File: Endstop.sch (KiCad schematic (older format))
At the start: 4 parts

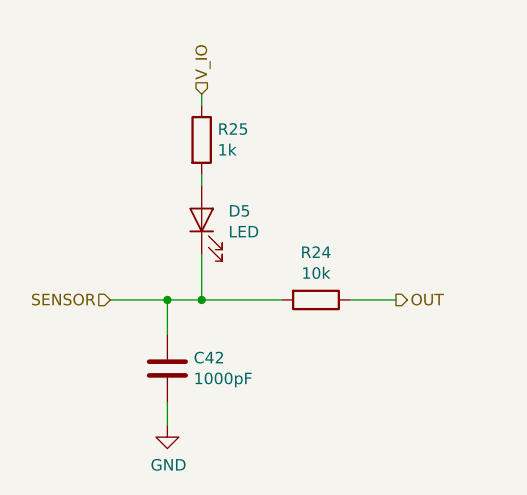
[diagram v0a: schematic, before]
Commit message: Carry over schematics updates from 2130 branch:   - fix z stop input resistor   - add extra fan connectors
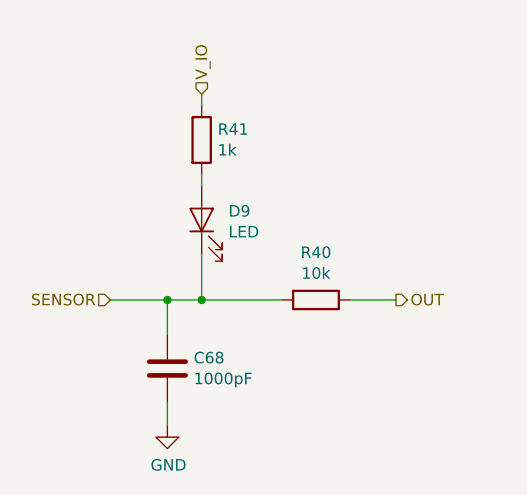
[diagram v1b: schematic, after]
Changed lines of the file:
@@
 AR Path="/5AC337B6/5ACE1C6D/5ACC8EC2/5ACC8647" Ref="R34"  Part="1"
 AR Path="/5AC337B6/5AD9F95A/5AD4BBBB/5ACC8647" Ref="R40"  Part="1"
-F 0 "R24" V 4093 2850 50  0000 C CNN
+F 0 "R40" V 4093 2850 50  0000 C CNN
 F 1 "10k" V 4184 2850 50  0000 C CNN
 F 2 "Resistor_SMD:R_0603_1608Metric" V 4230 2850 50  0001 C CNN
@@
 AR Path="/5AC337B6/5ACE1C6D/5ACC8EC2/5ACC864E" Ref="R35"  Part="1"
 AR Path="/5AC337B6/5AD9F95A/5AD4BBBB/5ACC864E" Ref="R41"  Part="1"
-F 0 "R25" H 3870 2196 50  0000 L CNN
+F 0 "R41" H 3870 2196 50  0000 L CNN
 F 1 "1k" H 3870 2105 50  0000 L CNN
 F 2 "Resistor_SMD:R_0603_1608Metric" V 3730 2150 50  0001 C CNN
@@
 AR Path="/5AC337B6/5ACE1C6D/5ACC8EC2/5ACC8655" Ref="D8"  Part="1"
 AR Path="/5AC337B6/5AD9F95A/5AD4BBBB/5ACC8655" Ref="D9"  Part="1"
-F 0 "D5" V 3838 2383 50  0000 R CNN
+F 0 "D9" V 3838 2383 50  0000 R CNN
 F 1 "LED" V 3747 2383 50  0000 R CNN
 F 2 "PrntrBoardV1:LED_0603_1608Metric" H 3800 2500 50  0001 C CNN
@@
 AR Path="/5AC337B6/5ACE1C6D/5ACC8EC2/5ACC865C" Ref="C56"  Part="1"
 AR Path="/5AC337B6/5AD9F95A/5AD4BBBB/5ACC865C" Ref="C68"  Part="1"
-F 0 "C42" H 3765 3196 50  0000 L CNN
+F 0 "C68" H 3765 3196 50  0000 L CNN
 F 1 "1000pF" H 3765 3105 50  0000 L CNN
 F 2 "Capacitor_SMD:C_0603_1608Metric" H 3688 3000 50  0001 C CNN
@@
 AR Path="/5AC337B6/5ACE1C6D/5ACC8EC2/5ACC8663" Ref="#PWR055"  Part="1"
 AR Path="/5AC337B6/5AD9F95A/5AD4BBBB/5ACC8663" Ref="#PWR064"  Part="1"
-F 0 "#PWR043" H 3650 3150 50  0001 C CNN
+F 0 "#PWR064" H 3650 3150 50  0001 C CNN
 F 1 "GND" H 3655 3227 50  0000 C CNN
 F 2 "" H 3650 3400 50  0001 C CNN

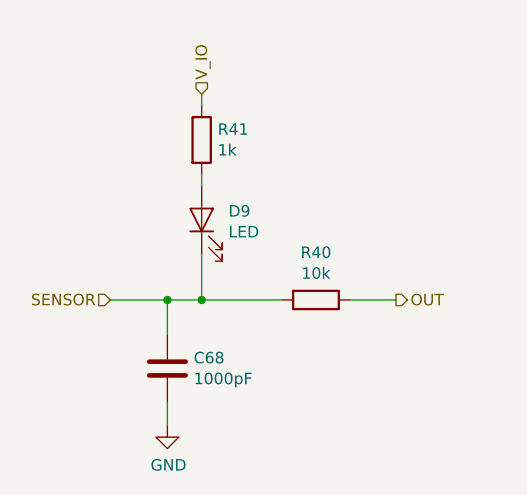
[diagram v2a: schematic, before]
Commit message: Add missing files from the TMC2130 branch.
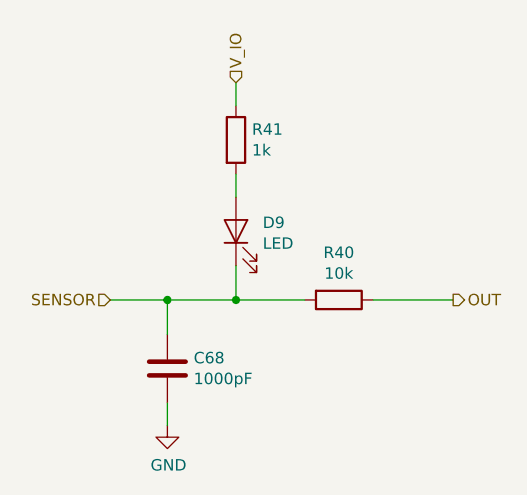
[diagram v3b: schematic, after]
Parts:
- C15: footprint Capacitor_SMD:C_0603_1608Metric -> PrntrBoardV1:C_0603_1608Metric
- R6, R7: footprint Resistor_SMD:R_0603_1608Metric -> PrntrBoardV1:R_0603_1608Metric
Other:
- moved on the sheet: D9, R40, R41
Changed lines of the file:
@@
 L Device:R R6
 U 1 1 5ACC8647
-P 4300 2850
+P 4400 2850
 AR Path="/5AC337B6/5ACBE919/5AD4BBBB/5ACC8647" Ref="R6"  Part="1"
 AR Path="/5AC337B6/5ACC0AA2/5ACC7E91/5ACC8647" Ref="R16"  Part="1"
@@
 AR Path="/5AC337B6/5ACE1C6D/5ACC8EC2/5ACC8647" Ref="R34"  Part="1"
 AR Path="/5AC337B6/5AD9F95A/5AD4BBBB/5ACC8647" Ref="R40"  Part="1"
-F 0 "R40" V 4093 2850 50  0000 C CNN
-F 1 "10k" V 4184 2850 50  0000 C CNN
-F 2 "Resistor_SMD:R_0603_1608Metric" V 4230 2850 50  0001 C CNN
-F 3 "~" H 4300 2850 50  0001 C CNN
-	1    4300 2850
+F 0 "R40" V 4193 2850 50  0000 C CNN
+F 1 "10k" V 4284 2850 50  0000 C CNN
+F 2 "PrntrBoardV1:R_0603_1608Metric" V 4330 2850 50  0001 C CNN
+F 3 "~" H 4400 2850 50  0001 C CNN
+	1    4400 2850
 	0    1    1    0
 $EndComp
@@
 L Device:R R7
 U 1 1 5ACC864E
-P 3800 2150
+P 3950 2150
 AR Path="/5AC337B6/5ACBE919/5AD4BBBB/5ACC864E" Ref="R7"  Part="1"
 AR Path="/5AC337B6/5ACC0AA2/5ACC7E91/5ACC864E" Ref="R17"  Part="1"
@@
 AR Path="/5AC337B6/5ACE1C6D/5ACC8EC2/5ACC864E" Ref="R35"  Part="1"
 AR Path="/5AC337B6/5AD9F95A/5AD4BBBB/5ACC864E" Ref="R41"  Part="1"
-F 0 "R41" H 3870 2196 50  0000 L CNN
-F 1 "1k" H 3870 2105 50  0000 L CNN
-F 2 "Resistor_SMD:R_0603_1608Metric" V 3730 2150 50  0001 C CNN
-F 3 "~" H 3800 2150 50  0001 C CNN
-	1    3800 2150
+F 0 "R41" H 4020 2196 50  0000 L CNN
+F 1 "1k" H 4020 2105 50  0000 L CNN
+F 2 "PrntrBoardV1:R_0603_1608Metric" V 3880 2150 50  0001 C CNN
+F 3 "~" H 3950 2150 50  0001 C CNN
+	1    3950 2150
 	1    0    0    -1
 $EndComp
@@
 L Device:LED D1
 U 1 1 5ACC8655
-P 3800 2500
+P 3950 2550
 AR Path="/5AC337B6/5ACBE919/5AD4BBBB/5ACC8655" Ref="D1"  Part="1"
 AR Path="/5AC337B6/5ACC0AA2/5ACC7E91/5ACC8655" Ref="D3"  Part="1"
@@
 AR Path="/5AC337B6/5ACE1C6D/5ACC8EC2/5ACC8655" Ref="D8"  Part="1"
 AR Path="/5AC337B6/5AD9F95A/5AD4BBBB/5ACC8655" Ref="D9"  Part="1"
-F 0 "D9" V 3838 2383 50  0000 R CNN
-F 1 "LED" V 3747 2383 50  0000 R CNN
-F 2 "PrntrBoardV1:LED_0603_1608Metric" H 3800 2500 50  0001 C CNN
-F 3 "~" H 3800 2500 50  0001 C CNN
-	1    3800 2500
+F 0 "D9" V 3988 2433 50  0000 R CNN
+F 1 "LED" V 3897 2433 50  0000 R CNN
+F 2 "PrntrBoardV1:LED_0603_1608Metric" H 3950 2550 50  0001 C CNN
+F 3 "~" H 3950 2550 50  0001 C CNN
+	1    3950 2550
 	0    -1   -1   0
 $EndComp
@@
 F 0 "C68" H 3765 3196 50  0000 L CNN
 F 1 "1000pF" H 3765 3105 50  0000 L CNN
-F 2 "Capacitor_SMD:C_0603_1608Metric" H 3688 3000 50  0001 C CNN
+F 2 "PrntrBoardV1:C_0603_1608Metric" H 3688 3000 50  0001 C CNN
 F 3 "~" H 3650 3150 50  0001 C CNN
 	1    3650 3150
@@
 	3650 3400 3650 3300
 Wire Wire Line
-	3800 2300 3800 2350
+	3950 2300 3950 2400
 Wire Wire Line
-	3800 2000 3800 1950
+	3950 2000 3950 1900
 Wire Wire Line
 	3650 3000 3650 2850
@@
 Text HLabel 3400 2850 0    50   Input ~ 0
 SENSOR
-Text HLabel 4650 2850 2    50   Output ~ 0
+Text HLabel 4900 2850 2    50   Output ~ 0
 OUT
-Text HLabel 3800 1950 1    50   Input ~ 0
+Text HLabel 3950 1900 1    50   Input ~ 0
 V_IO
 Wire Wire Line
-	3650 2850 3800 2850
+	3650 2850 3950 2850
 Wire Wire Line
-	3800 2650 3800 2850
-Connection ~ 3800 2850
+	3950 2700 3950 2850
 Wire Wire Line
-	3800 2850 4150 2850
+	4550 2850 4900 2850
 Wire Wire Line
-	4450 2850 4650 2850
+	4250 2850 3950 2850
+Connection ~ 3950 2850
 $EndSCHEMATC

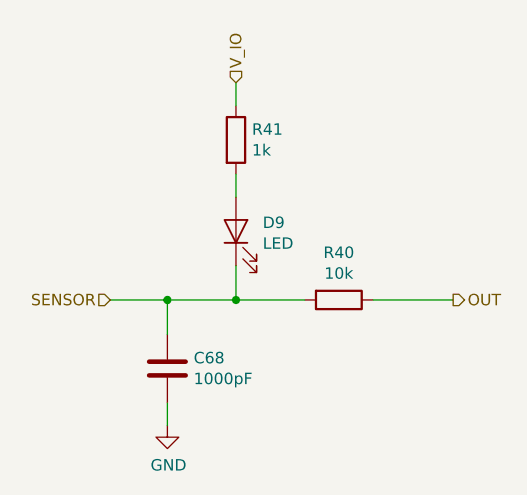
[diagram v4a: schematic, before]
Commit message: Reset schematics for tmc2660. Clean the board layout.
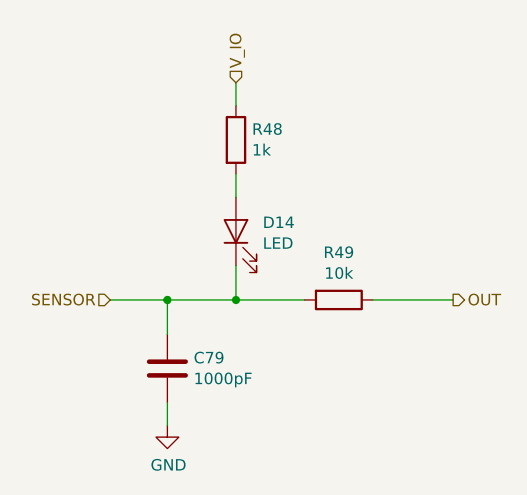
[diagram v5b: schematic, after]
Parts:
- renumbered C15 to C22, D1 to D5, R7 to R14, R6 to R15
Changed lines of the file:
@@
 $EndDescr
 $Comp
-L Device:R R6
+L Device:R R15
 U 1 1 5ACC8647
 P 4400 2850
-AR Path="/5AC337B6/5ACBE919/5AD4BBBB/5ACC8647" Ref="R6"  Part="1"
-AR Path="/5AC337B6/5ACC0AA2/5ACC7E91/5ACC8647" Ref="R16"  Part="1"
-AR Path="/5AC337B6/5ACC0AA2/5ACC8EC2/5ACC8647" Ref="R18"  Part="1"
-AR Path="/5AC337B6/5ACCA309/5ACC7E91/5ACC8647" Ref="R24"  Part="1"
-AR Path="/5AC337B6/5ACCA309/5ACC8EC2/5ACC8647" Ref="R26"  Part="1"
-AR Path="/5AC337B6/5ACE1C6D/5ACC7E91/5ACC8647" Ref="R32"  Part="1"
-AR Path="/5AC337B6/5ACE1C6D/5ACC8EC2/5ACC8647" Ref="R34"  Part="1"
-AR Path="/5AC337B6/5AD9F95A/5AD4BBBB/5ACC8647" Ref="R40"  Part="1"
-F 0 "R40" V 4193 2850 50  0000 C CNN
+AR Path="/5AC337B6/5ACBE919/5AD4BBBB/5ACC8647" Ref="R15"  Part="1"
+AR Path="/5AC337B6/5ACC0AA2/5ACC7E91/5ACC8647" Ref="R25"  Part="1"
+AR Path="/5AC337B6/5ACC0AA2/5ACC8EC2/5ACC8647" Ref="R27"  Part="1"
+AR Path="/5AC337B6/5ACCA309/5ACC7E91/5ACC8647" Ref="R33"  Part="1"
+AR Path="/5AC337B6/5ACCA309/5ACC8EC2/5ACC8647" Ref="R35"  Part="1"
+AR Path="/5AC337B6/5ACE1C6D/5ACC7E91/5ACC8647" Ref="R41"  Part="1"
+AR Path="/5AC337B6/5ACE1C6D/5ACC8EC2/5ACC8647" Ref="R43"  Part="1"
+AR Path="/5AC337B6/5AD9F95A/5AD4BBBB/5ACC8647" Ref="R49"  Part="1"
+F 0 "R49" V 4193 2850 50  0000 C CNN
 F 1 "10k" V 4284 2850 50  0000 C CNN
 F 2 "PrntrBoardV1:R_0603_1608Metric" V 4330 2850 50  0001 C CNN
@@
 $EndComp
 $Comp
-L Device:R R7
+L Device:R R14
 U 1 1 5ACC864E
 P 3950 2150
-AR Path="/5AC337B6/5ACBE919/5AD4BBBB/5ACC864E" Ref="R7"  Part="1"
-AR Path="/5AC337B6/5ACC0AA2/5ACC7E91/5ACC864E" Ref="R17"  Part="1"
-AR Path="/5AC337B6/5ACC0AA2/5ACC8EC2/5ACC864E" Ref="R19"  Part="1"
-AR Path="/5AC337B6/5ACCA309/5ACC7E91/5ACC864E" Ref="R25"  Part="1"
-AR Path="/5AC337B6/5ACCA309/5ACC8EC2/5ACC864E" Ref="R27"  Part="1"
-AR Path="/5AC337B6/5ACE1C6D/5ACC7E91/5ACC864E" Ref="R33"  Part="1"
-AR Path="/5AC337B6/5ACE1C6D/5ACC8EC2/5ACC864E" Ref="R35"  Part="1"
-AR Path="/5AC337B6/5AD9F95A/5AD4BBBB/5ACC864E" Ref="R41"  Part="1"
-F 0 "R41" H 4020 2196 50  0000 L CNN
+AR Path="/5AC337B6/5ACBE919/5AD4BBBB/5ACC864E" Ref="R14"  Part="1"
+AR Path="/5AC337B6/5ACC0AA2/5ACC7E91/5ACC864E" Ref="R24"  Part="1"
+AR Path="/5AC337B6/5ACC0AA2/5ACC8EC2/5ACC864E" Ref="R26"  Part="1"
+AR Path="/5AC337B6/5ACCA309/5ACC7E91/5ACC864E" Ref="R32"  Part="1"
+AR Path="/5AC337B6/5ACCA309/5ACC8EC2/5ACC864E" Ref="R34"  Part="1"
+AR Path="/5AC337B6/5ACE1C6D/5ACC7E91/5ACC864E" Ref="R40"  Part="1"
+AR Path="/5AC337B6/5ACE1C6D/5ACC8EC2/5ACC864E" Ref="R42"  Part="1"
+AR Path="/5AC337B6/5AD9F95A/5AD4BBBB/5ACC864E" Ref="R48"  Part="1"
+F 0 "R48" H 4020 2196 50  0000 L CNN
 F 1 "1k" H 4020 2105 50  0000 L CNN
 F 2 "PrntrBoardV1:R_0603_1608Metric" V 3880 2150 50  0001 C CNN
@@
 $EndComp
 $Comp
-L Device:LED D1
+L Device:LED D5
 U 1 1 5ACC8655
 P 3950 2550
-AR Path="/5AC337B6/5ACBE919/5AD4BBBB/5ACC8655" Ref="D1"  Part="1"
-AR Path="/5AC337B6/5ACC0AA2/5ACC7E91/5ACC8655" Ref="D3"  Part="1"
-AR Path="/5AC337B6/5ACC0AA2/5ACC8EC2/5ACC8655" Ref="D4"  Part="1"
-AR Path="/5AC337B6/5ACCA309/5ACC7E91/5ACC8655" Ref="D5"  Part="1"
-AR Path="/5AC337B6/5ACCA309/5ACC8EC2/5ACC8655" Ref="D6"  Part="1"
-AR Path="/5AC337B6/5ACE1C6D/5ACC7E91/5ACC8655" Ref="D7"  Part="1"
-AR Path="/5AC337B6/5ACE1C6D/5ACC8EC2/5ACC8655" Ref="D8"  Part="1"
-AR Path="/5AC337B6/5AD9F95A/5AD4BBBB/5ACC8655" Ref="D9"  Part="1"
-F 0 "D9" V 3988 2433 50  0000 R CNN
+AR Path="/5AC337B6/5ACBE919/5AD4BBBB/5ACC8655" Ref="D5"  Part="1"
+AR Path="/5AC337B6/5ACC0AA2/5ACC7E91/5ACC8655" Ref="D8"  Part="1"
+AR Path="/5AC337B6/5ACC0AA2/5ACC8EC2/5ACC8655" Ref="D9"  Part="1"
+AR Path="/5AC337B6/5ACCA309/5ACC7E91/5ACC8655" Ref="D10"  Part="1"
+AR Path="/5AC337B6/5ACCA309/5ACC8EC2/5ACC8655" Ref="D11"  Part="1"
+AR Path="/5AC337B6/5ACE1C6D/5ACC7E91/5ACC8655" Ref="D12"  Part="1"
+AR Path="/5AC337B6/5ACE1C6D/5ACC8EC2/5ACC8655" Ref="D13"  Part="1"
+AR Path="/5AC337B6/5AD9F95A/5AD4BBBB/5ACC8655" Ref="D14"  Part="1"
+F 0 "D14" V 3988 2433 50  0000 R CNN
 F 1 "LED" V 3897 2433 50  0000 R CNN
 F 2 "PrntrBoardV1:LED_0603_1608Metric" H 3950 2550 50  0001 C CNN
@@
 $EndComp
 $Comp
-L Device:C C15
+L Device:C C22
 U 1 1 5ACC865C
 P 3650 3150
-AR Path="/5AC337B6/5ACBE919/5AD4BBBB/5ACC865C" Ref="C15"  Part="1"
-AR Path="/5AC337B6/5ACC0AA2/5ACC7E91/5ACC865C" Ref="C29"  Part="1"
-AR Path="/5AC337B6/5ACC0AA2/5ACC8EC2/5ACC865C" Ref="C30"  Part="1"
-AR Path="/5AC337B6/5ACCA309/5ACC7E91/5ACC865C" Ref="C42"  Part="1"
-AR Path="/5AC337B6/5ACCA309/5ACC8EC2/5ACC865C" Ref="C43"  Part="1"
-AR Path="/5AC337B6/5ACE1C6D/5ACC7E91/5ACC865C" Ref="C55"  Part="1"
-AR Path="/5AC337B6/5ACE1C6D/5ACC8EC2/5ACC865C" Ref="C56"  Part="1"
-AR Path="/5AC337B6/5AD9F95A/5AD4BBBB/5ACC865C" Ref="C68"  Part="1"
-F 0 "C68" H 3765 3196 50  0000 L CNN
+AR Path="/5AC337B6/5ACBE919/5AD4BBBB/5ACC865C" Ref="C22"  Part="1"
+AR Path="/5AC337B6/5ACC0AA2/5ACC7E91/5ACC865C" Ref="C37"  Part="1"
+AR Path="/5AC337B6/5ACC0AA2/5ACC8EC2/5ACC865C" Ref="C38"  Part="1"
+AR Path="/5AC337B6/5ACCA309/5ACC7E91/5ACC865C" Ref="C51"  Part="1"
+AR Path="/5AC337B6/5ACCA309/5ACC8EC2/5ACC865C" Ref="C52"  Part="1"
+AR Path="/5AC337B6/5ACE1C6D/5ACC7E91/5ACC865C" Ref="C65"  Part="1"
+AR Path="/5AC337B6/5ACE1C6D/5ACC8EC2/5ACC865C" Ref="C66"  Part="1"
+AR Path="/5AC337B6/5AD9F95A/5AD4BBBB/5ACC865C" Ref="C79"  Part="1"
+F 0 "C79" H 3765 3196 50  0000 L CNN
 F 1 "1000pF" H 3765 3105 50  0000 L CNN
 F 2 "PrntrBoardV1:C_0603_1608Metric" H 3688 3000 50  0001 C CNN
@@
 $EndComp
 $Comp
-L power:GND #PWR019
+L power:GND #PWR030
 U 1 1 5ACC8663
 P 3650 3400
-AR Path="/5AC337B6/5ACBE919/5AD4BBBB/5ACC8663" Ref="#PWR019"  Part="1"
-AR Path="/5AC337B6/5ACC0AA2/5ACC7E91/5ACC8663" Ref="#PWR032"  Part="1"
-AR Path="/5AC337B6/5ACC0AA2/5ACC8EC2/5ACC8663" Ref="#PWR033"  Part="1"
-AR Path="/5AC337B6/5ACCA309/5ACC7E91/5ACC8663" Ref="#PWR043"  Part="1"
-AR Path="/5AC337B6/5ACCA309/5ACC8EC2/5ACC8663" Ref="#PWR044"  Part="1"
-AR Path="/5AC337B6/5ACE1C6D/5ACC7E91/5ACC8663" Ref="#PWR054"  Part="1"
-AR Path="/5AC337B6/5ACE1C6D/5ACC8EC2/5ACC8663" Ref="#PWR055"  Part="1"
-AR Path="/5AC337B6/5AD9F95A/5AD4BBBB/5ACC8663" Ref="#PWR064"  Part="1"
-F 0 "#PWR064" H 3650 3150 50  0001 C CNN
+AR Path="/5AC337B6/5ACBE919/5AD4BBBB/5ACC8663" Ref="#PWR030"  Part="1"
+AR Path="/5AC337B6/5ACC0AA2/5ACC7E91/5ACC8663" Ref="#PWR043"  Part="1"
+AR Path="/5AC337B6/5ACC0AA2/5ACC8EC2/5ACC8663" Ref="#PWR044"  Part="1"
+AR Path="/5AC337B6/5ACCA309/5ACC7E91/5ACC8663" Ref="#PWR054"  Part="1"
+AR Path="/5AC337B6/5ACCA309/5ACC8EC2/5ACC8663" Ref="#PWR055"  Part="1"
+AR Path="/5AC337B6/5ACE1C6D/5ACC7E91/5ACC8663" Ref="#PWR065"  Part="1"
+AR Path="/5AC337B6/5ACE1C6D/5ACC8EC2/5ACC8663" Ref="#PWR066"  Part="1"
+AR Path="/5AC337B6/5AD9F95A/5AD4BBBB/5ACC8663" Ref="#PWR075"  Part="1"
+F 0 "#PWR075" H 3650 3150 50  0001 C CNN
 F 1 "GND" H 3655 3227 50  0000 C CNN
 F 2 "" H 3650 3400 50  0001 C CNN
